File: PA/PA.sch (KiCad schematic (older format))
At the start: 75 parts, among them J1 Conn_Coaxial, J2 Conn_01x02, J3 Conn_Coaxial, J4 Conn_01x02, J5 Conn_01x02, J6 Conn_01x01, J7 Conn_01x01, J8 Conn_01x01, J9 Conn_01x01, Q1 2N3904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

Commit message: Add transmit disable switch
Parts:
- added C38: 100 nF, Capacitors_THT:C_Disc_D5.0mm_W2.5mm_P2.50mm, symbol C_Small
- added C39: 1 nF, Capacitors_THT:C_Disc_D5.0mm_W2.5mm_P2.50mm, symbol C_Small
- added D10, D11, D8, D9: ZENER, Diodes_THT:D_DO-41_SOD81_P7.62mm_Horizontal, symbol D_Zener
- added J27, J28: Conn_01x01, Connectors:1pin, symbol Conn_01x01
- added R16: 470R, Resistors_THT:R_Axial_DIN0207_L6.3mm_D2.5mm_P7.62mm_Horizontal, symbol R
- C4: value 1 nF -> 10 nF
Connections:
- net +28V: now also C38.1
- net GND: now also C38.2, C39.2, D10.2 (A), D11.2 (A), J28.1 (Pin_1)
- net at C2.2, C3.1, C4.2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: now also R16.1
- net at C11.1, C13.2, C20.1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: now also D8.1 (K)
- net at C12.1, C14.2, C20.2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: now also D9.1 (K)
- net at D7.1 (K), Q5.1 (G), Q6.3 (C)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: now also C39.1
- new net: D10.1 (K), D8.2 (A)
- new net: D11.1 (K), D9.2 (A)
- new net: J27.1 (Pin_1), R16.2
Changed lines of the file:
@@
 P 2700 2350
 F 0 "C4" H 2710 2420 50  0000 L CNN
-F 1 "1 nF" H 2710 2270 50  0000 L CNN
+F 1 "10 nF" H 2710 2270 50  0000 L CNN
 F 2 "Capacitors_THT:C_Disc_D5.0mm_W2.5mm_P2.50mm" H 2700 2350 50  0001 C CNN
 F 3 "" H 2700 2350 50  0001 C CNN
@@
 $EndComp
 $Comp
-L GND #PWR32
+L GND #PWR33
 U 1 1 5C63A13E
 P 6450 5350
-F 0 "#PWR32" H 6450 5100 50  0001 C CNN
+F 0 "#PWR33" H 6450 5100 50  0001 C CNN
 F 1 "GND" H 6450 5200 50  0000 C CNN
 F 2 "" H 6450 5350 50  0001 C CNN
@@
 $EndComp
 $Comp
-L GND #PWR42
+L GND #PWR45
 U 1 1 5C63CACF
 P 7900 4050
-F 0 "#PWR42" H 7900 3800 50  0001 C CNN
+F 0 "#PWR45" H 7900 3800 50  0001 C CNN
 F 1 "GND" H 7900 3900 50  0000 C CNN
 F 2 "" H 7900 4050 50  0001 C CNN
@@
 $EndComp
 $Comp
-L GND #PWR36
+L GND #PWR38
 U 1 1 5C63B4B9
 P 6900 6300
-F 0 "#PWR36" H 6900 6050 50  0001 C CNN
+F 0 "#PWR38" H 6900 6050 50  0001 C CNN
 F 1 "GND" H 6900 6150 50  0000 C CNN
 F 2 "" H 6900 6300 50  0001 C CNN
@@
 $EndComp
 $Comp
-L +5V #PWR35
+L +5V #PWR37
 U 1 1 5C63B9B6
 P 6900 5750
-F 0 "#PWR35" H 6900 5600 50  0001 C CNN
+F 0 "#PWR37" H 6900 5600 50  0001 C CNN
 F 1 "+5V" H 6900 5890 50  0000 C CNN
 F 2 "" H 6900 5750 50  0001 C CNN
@@
 $EndComp
 $Comp
-L GND #PWR38
+L GND #PWR40
 U 1 1 5C63BE2B
 P 7200 6300
-F 0 "#PWR38" H 7200 6050 50  0001 C CNN
+F 0 "#PWR40" H 7200 6050 50  0001 C CNN
 F 1 "GND" H 7200 6150 50  0000 C CNN
 F 2 "" H 7200 6300 50  0001 C CNN
@@
 $EndComp
 $Comp
-L GND #PWR41
+L GND #PWR44
 U 1 1 5C63CB31
 P 7600 6300
-F 0 "#PWR41" H 7600 6050 50  0001 C CNN
+F 0 "#PWR44" H 7600 6050 50  0001 C CNN
 F 1 "GND" H 7600 6150 50  0000 C CNN
 F 2 "" H 7600 6300 50  0001 C CNN
@@
 $EndComp
 $Comp
-L +28V #PWR37
+L +28V #PWR39
 U 1 1 5C63CFA3
 P 7150 1200
-F 0 "#PWR37" H 7150 1050 50  0001 C CNN
+F 0 "#PWR39" H 7150 1050 50  0001 C CNN
 F 1 "+28V" H 7150 1350 50  0000 C CNN
 F 2 "" H 7400 1250 50  0001 C CNN
@@
 $EndComp
 $Comp
-L GND #PWR39
+L GND #PWR42
 U 1 1 5C63EA3A
 P 7350 1050
-F 0 "#PWR39" H 7350 800 50  0001 C CNN
+F 0 "#PWR42" H 7350 800 50  0001 C CNN
 F 1 "GND" H 7350 900 50  0000 C CNN
 F 2 "" H 7350 1050 50  0001 C CNN
@@
 $EndComp
 $Comp
-L GND #PWR40
+L GND #PWR43
 U 1 1 5C642161
 P 7600 2200
-F 0 "#PWR40" H 7600 1950 50  0001 C CNN
+F 0 "#PWR43" H 7600 1950 50  0001 C CNN
 F 1 "GND" H 7600 2050 50  0000 C CNN
 F 2 "" H 7600 2200 50  0001 C CNN
@@
 $EndComp
 $Comp
-L +28V #PWR33
+L +28V #PWR34
 U 1 1 5C6432E0
 P 6550 2200
-F 0 "#PWR33" H 6550 2050 50  0001 C CNN
+F 0 "#PWR34" H 6550 2050 50  0001 C CNN
 F 1 "+28V" H 6550 2350 50  0000 C CNN
 F 2 "" H 6800 2250 50  0001 C CNN
@@
 $EndComp
 $Comp
-L GND #PWR43
+L GND #PWR46
 U 1 1 5C643921
 P 8050 2250
-F 0 "#PWR43" H 8050 2000 50  0001 C CNN
+F 0 "#PWR46" H 8050 2000 50  0001 C CNN
 F 1 "GND" H 8050 2100 50  0000 C CNN
 F 2 "" H 8050 2250 50  0001 C CNN
@@
 $EndComp
 $Comp
-L GND #PWR31
+L GND #PWR32
 U 1 1 5C644E60
 P 6250 800
-F 0 "#PWR31" H 6250 550 50  0001 C CNN
+F 0 "#PWR32" H 6250 550 50  0001 C CNN
 F 1 "GND" H 6250 650 50  0000 C CNN
 F 2 "" H 6250 800 50  0001 C CNN
@@
 $EndComp
 $Comp
-L GND #PWR34
+L GND #PWR36
 U 1 1 5C6458BD
 P 6900 850
-F 0 "#PWR34" H 6900 600 50  0001 C CNN
+F 0 "#PWR36" H 6900 600 50  0001 C CNN
 F 1 "GND" H 6900 700 50  0000 C CNN
 F 2 "" H 6900 850 50  0001 C CNN
@@
 	2700 2100 2700 2250
 Wire Wire Line
-	2700 2750 2700 2450
+	2700 2450 2700 2950
 Connection ~ 2700 2750
 Wire Wire Line
@@
 	7600 1600 7600 1700
 Wire Wire Line
-	7450 1600 7450 1650
+	7450 1600 7450 1750
 Wire Wire Line
 	7450 1650 7700 1650
@@
 Text Notes 7800 6950 0    60   ~ 0
 WA2EBY amplifier, in KiCAD by KW4TI, CC-BY-SA 4.0\nadded overcurrent protection for PA transistors
+$Comp
+L C_Small C38
+U 1 1 5C645E45
+P 8350 900
+F 0 "C38" H 8360 970 50  0000 L CNN
+F 1 "100 nF" H 8360 820 50  0000 L CNN
+F 2 "Capacitors_THT:C_Disc_D5.0mm_W2.5mm_P2.50mm" H 8350 900 50  0001 C CNN
+F 3 "" H 8350 900 50  0001 C CNN
+	1    8350 900
+	1    0    0    -1
+$EndComp
+$Comp
+L +28V #PWR47
+U 1 1 5C646305
+P 8350 750
+F 0 "#PWR47" H 8350 600 50  0001 C CNN
+F 1 "+28V" H 8350 900 50  0000 C CNN
+F 2 "" H 8600 800 50  0001 C CNN
+F 3 "" H 8600 800 50  0001 C CNN
+	1    8350 750
+	1    0    0    -1
+$EndComp
+$Comp
+L GND #PWR48
+U 1 1 5C6463F4
+P 8350 1100
+F 0 "#PWR48" H 8350 850 50  0001 C CNN
+F 1 "GND" H 8350 950 50  0000 C CNN
+F 2 "" H 8350 1100 50  0001 C CNN
+F 3 "" H 8350 1100 50  0001 C CNN
+	1    8350 1100
+	1    0    0    -1
+$EndComp
+Wire Wire Line
+	8350 1100 8350 1000
+Wire Wire Line
+	8350 750  8350 800
+$Comp
+L C_Small C39
+U 1 1 5C6469B5
+P 7300 1950
+F 0 "C39" H 7310 2020 50  0000 L CNN
+F 1 "1 nF" H 7310 1870 50  0000 L CNN
+F 2 "Capacitors_THT:C_Disc_D5.0mm_W2.5mm_P2.50mm" H 7300 1950 50  0001 C CNN
+F 3 "" H 7300 1950 50  0001 C CNN
+	1    7300 1950
+	1    0    0    -1
+$EndComp
+$Comp
+L GND #PWR41
+U 1 1 5C646C9F
+P 7300 2200
+F 0 "#PWR41" H 7300 1950 50  0001 C CNN
+F 1 "GND" H 7300 2050 50  0000 C CNN
+F 2 "" H 7300 2200 50  0001 C CNN
+F 3 "" H 7300 2200 50  0001 C CNN
+	1    7300 2200
+	1    0    0    -1
+$EndComp
+Wire Wire Line
+	7300 2200 7300 2050
+Wire Wire Line
+	7300 1850 7300 1750
+Wire Wire Line
+	7300 1750 7450 1750
+Connection ~ 7450 1650
+$Comp
+L D_Zener D8
+U 1 1 5C64607F
+P 5800 3750
+F 0 "D8" H 5800 3850 50  0000 C CNN
+F 1 "ZENER" H 5800 3650 50  0000 C CNN
+F 2 "Diodes_THT:D_DO-41_SOD81_P7.62mm_Horizontal" H 5800 3750 50  0001 C CNN
+F 3 "" H 5800 3750 50  0001 C CNN
+	1    5800 3750
+	0    1    1    0
+$EndComp
+Wire Wire Line
+	5800 3600 5800 3550
+Connection ~ 5800 3550
+$Comp
+L GND #PWR31
+U 1 1 5C646488
+P 6000 4150
+F 0 "#PWR31" H 6000 3900 50  0001 C CNN
+F 1 "GND" H 6000 4000 50  0000 C CNN
+F 2 "" H 6000 4150 50  0001 C CNN
+F 3 "" H 6000 4150 50  0001 C CNN
+	1    6000 4150
+	1    0    0    -1
+$EndComp
+Wire Wire Line
+	5800 4050 5800 3900
+$Comp
+L D_Zener D9
+U 1 1 5C646770
+P 6600 4200
+F 0 "D9" H 6600 4300 50  0000 C CNN
+F 1 "ZENER" H 6600 4100 50  0000 C CNN
+F 2 "Diodes_THT:D_DO-41_SOD81_P7.62mm_Horizontal" H 6600 4200 50  0001 C CNN
+F 3 "" H 6600 4200 50  0001 C CNN
+	1    6600 4200
+	0    1    1    0
+$EndComp
+Wire Wire Line
+	6600 4050 6600 3950
+Connection ~ 6600 3950
+$Comp
+L GND #PWR35
+U 1 1 5C646B94
+P 6600 4850
+F 0 "#PWR35" H 6600 4600 50  0001 C CNN
+F 1 "GND" H 6600 4700 50  0000 C CNN
+F 2 "" H 6600 4850 50  0001 C CNN
+F 3 "" H 6600 4850 50  0001 C CNN
+	1    6600 4850
+	1    0    0    -1
+$EndComp
+Wire Wire Line
+	6600 4450 6600 4350
+$Comp
+L D_Zener D11
+U 1 1 5C648AA2
+P 6600 4600
+F 0 "D11" H 6600 4700 50  0000 C CNN
+F 1 "ZENER" H 6600 4500 50  0000 C CNN
+F 2 "Diodes_THT:D_DO-41_SOD81_P7.62mm_Horizontal" H 6600 4600 50  0001 C CNN
+F 3 "" H 6600 4600 50  0001 C CNN
+	1    6600 4600
+	0    1    1    0
+$EndComp
+Wire Wire Line
+	6600 4750 6600 4850
+$Comp
+L D_Zener D10
+U 1 1 5C648EFC
+P 6000 3900
+F 0 "D10" H 6000 4000 50  0000 C CNN
+F 1 "ZENER" H 6000 3800 50  0000 C CNN
+F 2 "Diodes_THT:D_DO-41_SOD81_P7.62mm_Horizontal" H 6000 3900 50  0001 C CNN
+F 3 "" H 6000 3900 50  0001 C CNN
+	1    6000 3900
+	0    1    1    0
+$EndComp
+Wire Wire Line
+	5800 4050 5900 4050
+Wire Wire Line
+	5900 4050 5900 3750
+Wire Wire Line
+	5900 3750 6000 3750
+Wire Wire Line
+	6000 4050 6000 4150
+$Comp
+L R R16
+U 1 1 5C649B62
+P 2700 3100
+F 0 "R16" V 2780 3100 50  0000 C CNN
+F 1 "470R" V 2700 3100 50  0000 C CNN
+F 2 "Resistors_THT:R_Axial_DIN0207_L6.3mm_D2.5mm_P7.62mm_Horizontal" V 2630 3100 50  0001 C CNN
+F 3 "" H 2700 3100 50  0001 C CNN
+	1    2700 3100
+	1    0    0    -1
+$EndComp
+$Comp
+L Conn_01x01 J27
+U 1 1 5C649F82
+P 2700 3500
+F 0 "J27" H 2700 3600 50  0000 C CNN
+F 1 "Conn_01x01" H 2700 3400 50  0000 C CNN
+F 2 "Connectors:1pin" H 2700 3500 50  0001 C CNN
+F 3 "" H 2700 3500 50  0001 C CNN
+	1    2700 3500
+	0    1    1    0
+$EndComp
+Wire Wire Line
+	2700 3250 2700 3300
+$Comp
+L Conn_01x01 J28
+U 1 1 5C64A312
+P 2900 3100
+F 0 "J28" H 2900 3200 50  0000 C CNN
+F 1 "Conn_01x01" H 2900 3000 50  0000 C CNN
+F 2 "Connectors:1pin" H 2900 3100 50  0001 C CNN
+F 3 "" H 2900 3100 50  0001 C CNN
+	1    2900 3100
+	-1   0    0    1
+$EndComp
+Wire Wire Line
+	3100 3100 3200 3100
+Connection ~ 3200 3100
 $EndSCHEMATC

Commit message: Tightened up components
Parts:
- R10, R6, R7, R8: footprint Resistors_THT:R_Axial_DIN0411_L9.9mm_D3.6mm_P12.70mm_Horizontal -> Resistors_THT:R_Axial_DIN0207_L6.3mm_D2.5mm_P10.16mm_Horizontal

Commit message: Changed overcurrent circuit...
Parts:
- removed C39: 1 nF, Capacitors_THT:C_Disc_D5.0mm_W2.5mm_P2.50mm, symbol C_Small
- removed D7: 1N4744A, Diodes_THT:D_DO-41_SOD81_P7.62mm_Horizontal, symbol D_Zener
- removed Q5: IRF510N, TO_SOT_Packages_THT:TO-220-3_Vertical, symbol IRF540N
- removed Q6: 2N3904, TO_SOT_Packages_THT:TO-92_Molded_Narrow, symbol 2N3904
- added D7: LED, LEDs:LED_D3.0mm, symbol LED
- added Q5: TIP42, TO_SOT_Packages_THT:TO-220_Vertical, symbol TIP42
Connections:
- net +28V: now also JP4.1, Q4.1 (E), R14.2, Q5.3 (E); no longer JP4.3, R15.1
- net GND: now also D7.1 (K); no longer R12.1
- net PASUPPLY: now also R14.1, Q5.1 (B); no longer JP4.2, R13.2
- net at R15.2: now also D7.2 (A)
- net at Q4.2 (B): now also R12.2; no longer R14.2
- net at Q4.3 (C): now also JP4.3; no longer R12.2
- new net: Q5.2 (C), R12.1, R15.1
- new net BIASSUPPLY: JP4.2, R13.2
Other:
- moved on the sheet: JP4, Q4, R14

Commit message: Added via fences
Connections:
- net AMPINPUT: now also RLY1.8 (NO); no longer RLY1.4 (NO)
- net at C1.1, J1.1 (In), J2.1 (Pin_1): now also RLY1.6 (Pole); no longer RLY1.2 (Pole)
- net at J3.1 (In), J5.1 (Pin_1): now also RLY1.2 (Pole); no longer RLY1.6 (Pole)
- net at JP5.2: now also RLY1.4 (NO); no longer RLY1.8 (NO)
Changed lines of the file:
@@
 	1    0    0    -1
 $EndComp
-Text GLabel 4950 2250 2    60   Input ~ 0
+Text GLabel 4800 1900 2    60   Input ~ 0
 AMPINPUT
 Text GLabel 8200 3050 0    60   Input ~ 0
@@
 	3900 1200 3900 1400
 Wire Wire Line
-	3650 550  3650 1800
+	3650 550  3650 1000
 Wire Wire Line
 	3650 1000 3750 1000
@@
 	4850 1700 4700 1700
 Wire Wire Line
-	4700 2250 4950 2250
+	4700 2250 5350 2250
 Wire Wire Line
 	2350 2100 2950 2100
@@
 Connection ~ 3400 2100
 Wire Wire Line
-	3550 2150 3650 2150
-Wire Wire Line
-	3550 1450 3550 2150
-Wire Wire Line
-	1550 1450 3550 1450
+	1550 1450 3450 1450
 Connection ~ 1550 1900
-Wire Wire Line
-	4700 1900 5200 1900
 Wire Wire Line
 	1550 4950 1550 4850
@@
 Wire Wire Line
 	1800 1000 1800 1450
-Connection ~ 1800 1450
 Wire Wire Line
 	1850 1250 1850 1100
@@
 Wire Wire Line
 	3650 550  3800 550
-Connection ~ 3650 1000
 Wire Wire Line
 	3750 750  3750 650
@@
 Wire Wire Line
 	8250 4100 8250 3800
-Wire Wire Line
-	5400 1250 5200 1250
-Wire Wire Line
-	5200 1250 5200 1900
 Wire Wire Line
 	5300 800  5500 800
@@
 Wire Wire Line
 	6850 2650 6850 2800
+Wire Wire Line
+	5400 1250 5350 1250
+Wire Wire Line
+	5350 1250 5350 2250
+Wire Wire Line
+	4800 1900 4700 1900
+Connection ~ 1800 1450
+Wire Wire Line
+	3550 2150 3650 2150
+Wire Wire Line
+	3650 1800 3450 1800
+Wire Wire Line
+	3450 1800 3450 1450
+Wire Wire Line
+	3550 2150 3550 750
+Wire Wire Line
+	3550 750  3650 750
+Connection ~ 3650 750
 $EndSCHEMATC

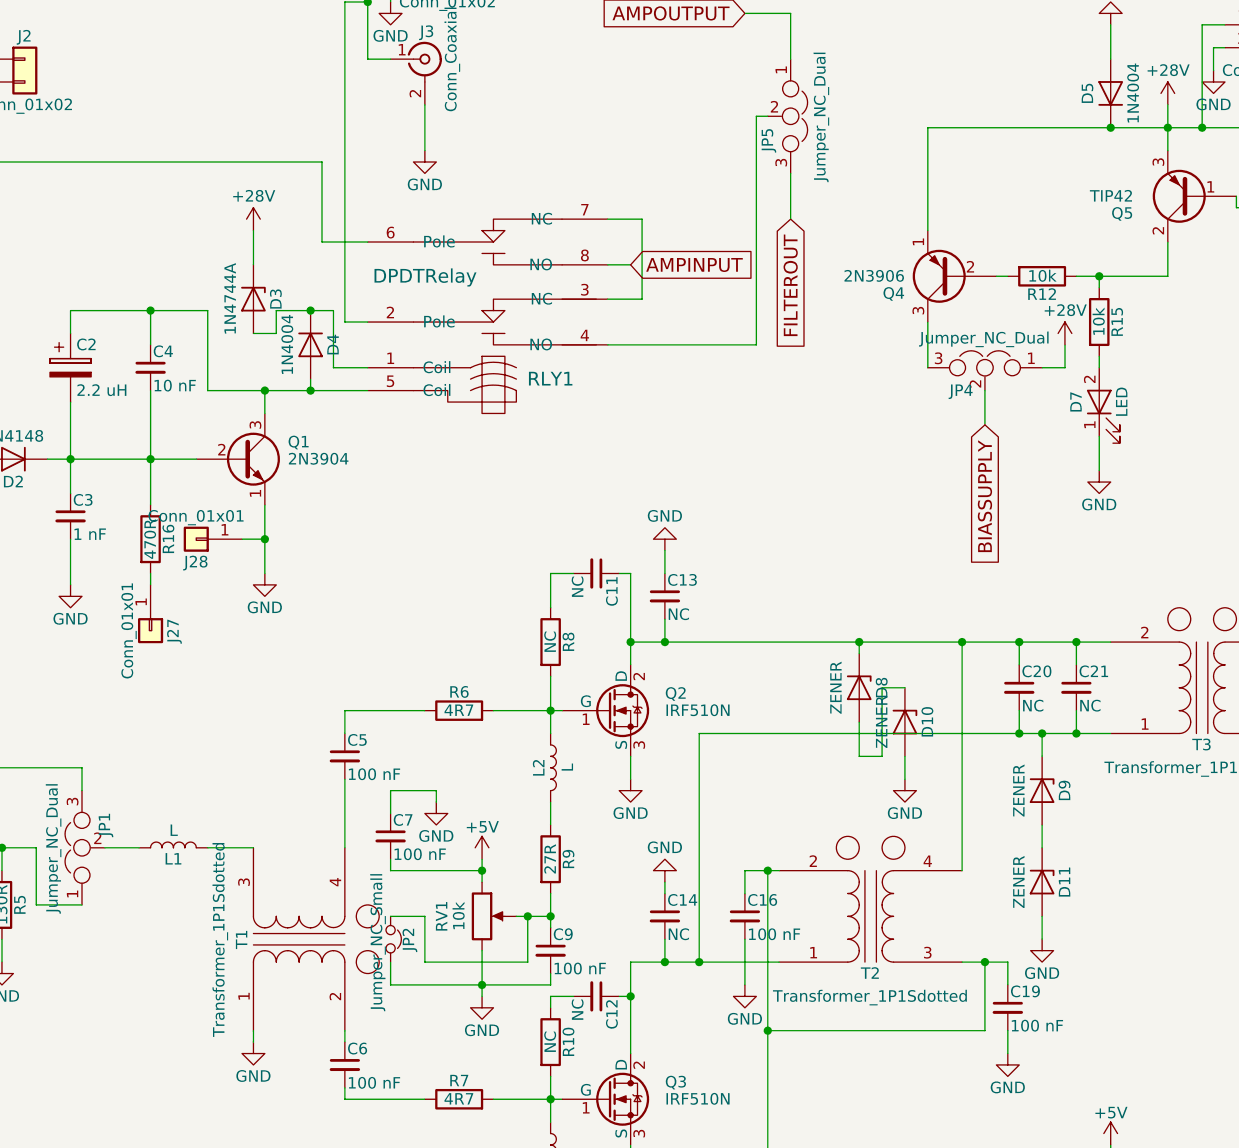
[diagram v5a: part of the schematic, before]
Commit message: Added more convenient pads for TO220 devices
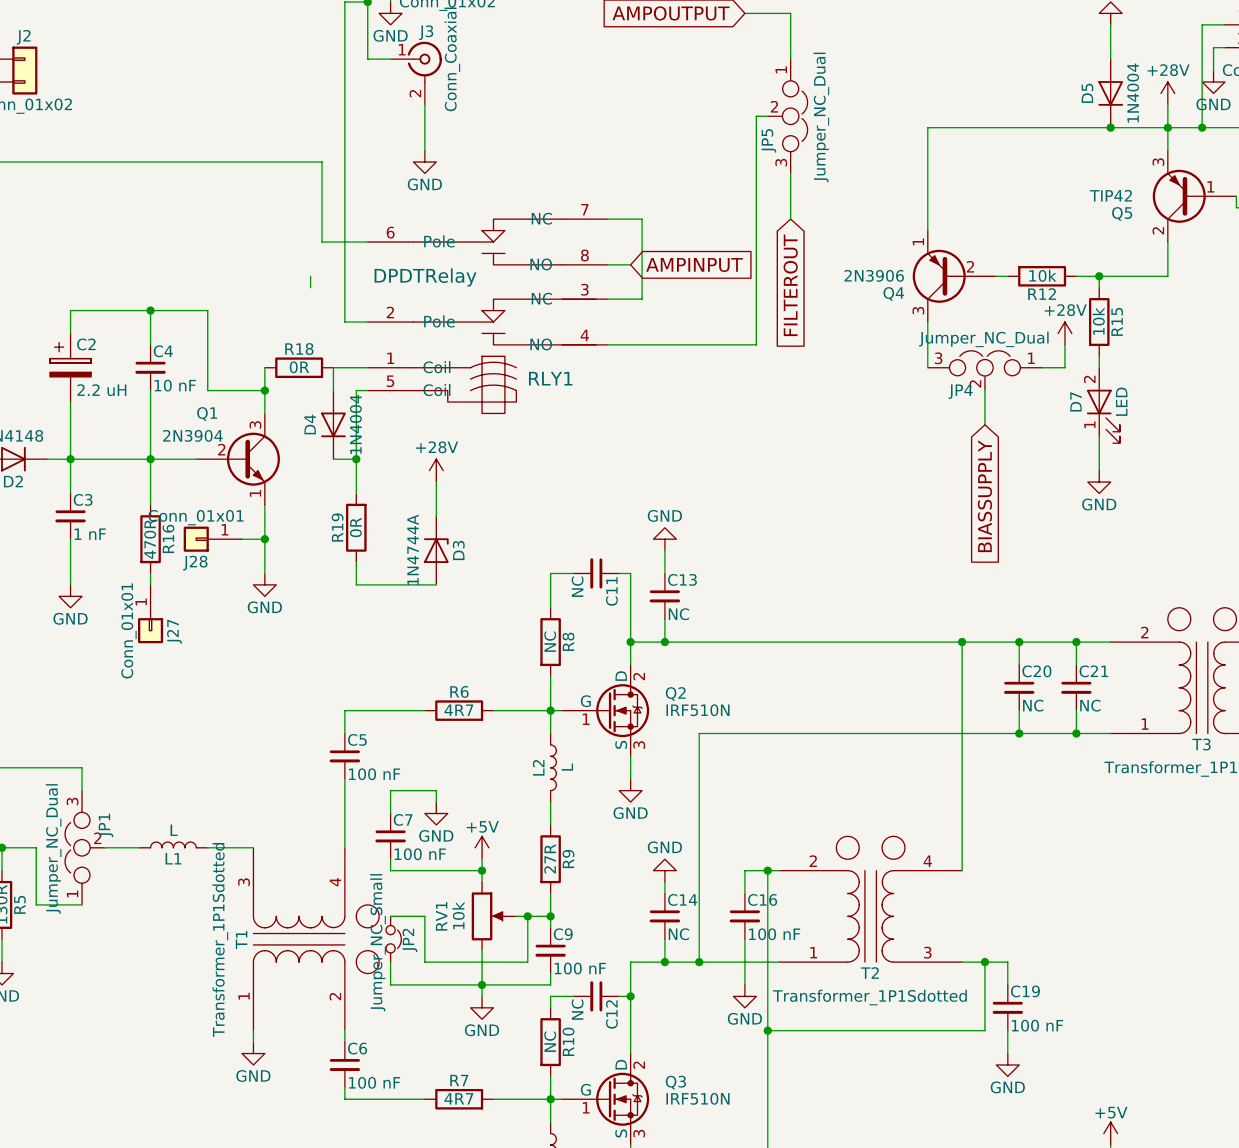
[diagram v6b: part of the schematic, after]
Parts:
- removed D10, D11, D8, D9: ZENER, Diodes_THT:D_DO-41_SOD81_P7.62mm_Horizontal, symbol D_Zener
- added R18, R19: 0R, Resistors_THT:R_Axial_DIN0207_L6.3mm_D2.5mm_P7.62mm_Horizontal, symbol R
- Q2, Q3: footprint TO_SOT_Packages_THT:TO-220-3_Vertical -> PA:TO-220-3_Vertical_WithPads
- Q5: footprint TO_SOT_Packages_THT:TO-220_Vertical -> PA:TO-220-3_Vertical_WithPads
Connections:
- net at C2.1, C4.1, Q1.3 (C): now also R18.1; no longer D4.2 (A), RLY1.5 (Coil)
- new net: D4.1 (K), R19.2, RLY1.5 (Coil)
- new net: D4.2 (A), R18.2, RLY1.1 (Coil)
- new net: D3.2 (A), R19.1
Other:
- moved on the sheet: D3, D4
